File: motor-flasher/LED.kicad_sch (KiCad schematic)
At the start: 5 parts, among them U9 PCF8574T_3_518

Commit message: Beginning Layout Process
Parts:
- added C11: 100nF, Capacitor_SMD:C_0402_1005Metric, symbol Device:C
- DS1: footprint revparts2:LCD_LCM-S01602DTR_A -> LCM-S01602DTR_A:LCD_LCM-S01602DTR_A
- R13: value 10k -> 220
- U9: footprint revparts2:SOIC127P1032X265-16N -> Motor-Flasher:SOIC127P1032X265-16N
- VR1: footprint revparts3:POT_3362P -> Motor-Flasher:POT_3362P
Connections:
- net +3.3V: now also C11.2
- net GND: now also C11.1
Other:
- moved on the sheet: C14, DS1, R13, U9, VR1

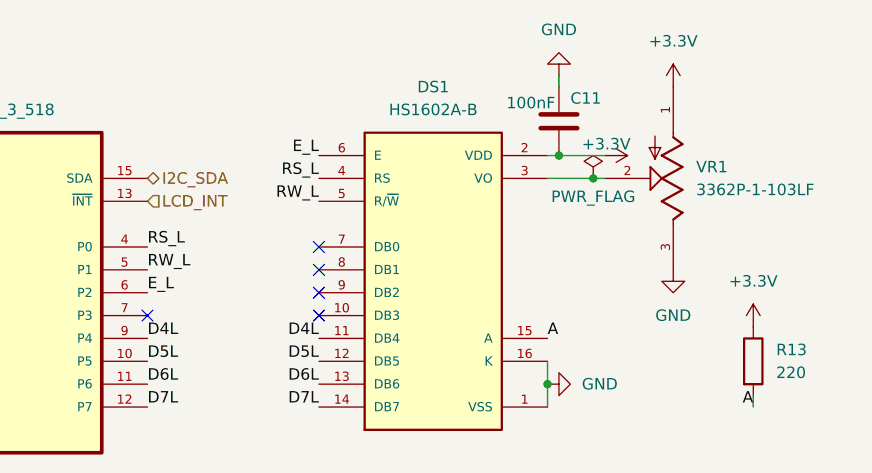
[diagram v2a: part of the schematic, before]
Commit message: Removed ERC Errors and Warnings
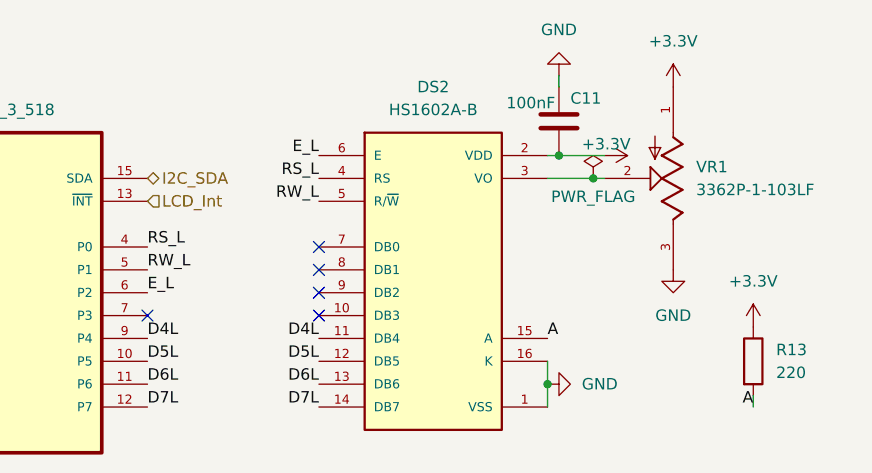
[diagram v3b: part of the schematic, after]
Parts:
- removed DS1: HS1602A-B, LCM-S01602DTR_A:LCD_LCM-S01602DTR_A, symbol LCM-S01602DTR_A:LCM-S01602DTR_A
- removed VR1: 3362P-1-103LF, Motor-Flasher:POT_3362P, symbol 3362P-1-103LF:3362P-1-103LF
- added DS2: HS1602A-B, LCM-S01602DTR_A:LCD_LCM-S01602DTR_A, symbol Motor_Flasher_Modified:LCM-S01602DTR_A
- added VR1: 3362P-1-103LF, Motor-Flasher:POT_3362P, symbol Motor_Flasher_Modified:3362P-1-103LF
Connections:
- net +3.3V: now also DS2.2 (VDD), VR1.1
- net A: now also DS2.15 (A)
- net D4L: now also DS2.11 (DB4)
- net D5L: now also DS2.12 (DB5)
- net D6L: now also DS2.13 (DB6)
- net D7L: now also DS2.14 (DB7)
- net E_L: now also DS2.6 (E)
- net GND: now also DS2.1 (VSS), DS2.16 (K), VR1.3
- net RS_L: now also DS2.4 (RS)
- net RW_L: now also DS2.5 (R/~{W})
- net LCD_INT renamed LCD_Int
- new net: DS2.3 (VO), VR1.2

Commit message: Rough Placement and Design
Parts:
- DS2: footprint LCM-S01602DTR_A:LCD_LCM-S01602DTR_A -> Motor-Flasher:LCD_LCM-S01602DTR_A
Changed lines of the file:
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@@
 			)
 		)
-		(property "Footprint" "LCM-S01602DTR_A:LCD_LCM-S01602DTR_A"
+		(property "Footprint" "Motor-Flasher:LCD_LCM-S01602DTR_A"
 			(at 142.24 90.17 0)
 			(effects
